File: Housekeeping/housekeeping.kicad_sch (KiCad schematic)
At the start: 4 parts, among them P7803B-1000R1 P7803B-1000, P7812B-1000R1 490-P7812B-1000

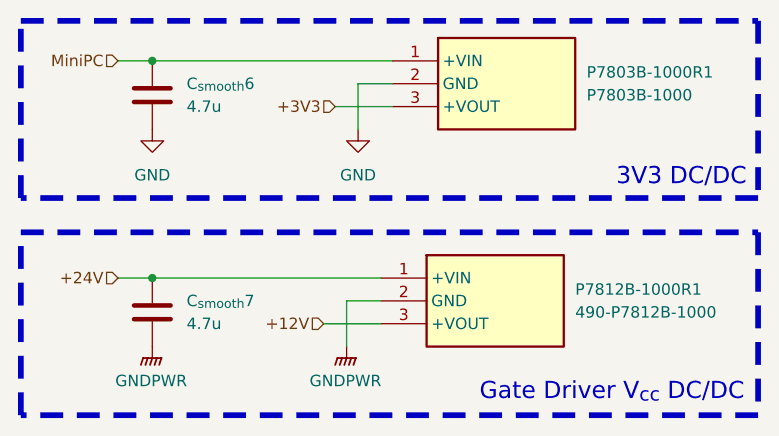
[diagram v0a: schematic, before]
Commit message: still need to finish housekeeping power supply footprints
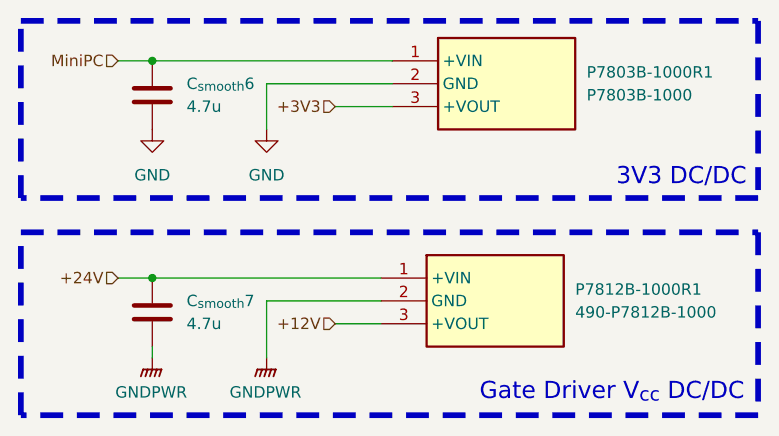
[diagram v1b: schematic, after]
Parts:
- P7803B-1000R1, P7812B-1000R1: footprint Robomaster_ICs:P7812B1000 -> Robomaster_ICs:P78B-1000R
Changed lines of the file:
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@@
 	(wire
 		(pts
-			(xy 130.81 106.68) (xy 130.81 101.6)
+			(xy 121.92 107.95) (xy 121.92 101.6)
 		)
 		(stroke
@@
 	(wire
 		(pts
-			(xy 132.08 77.47) (xy 132.08 82.55)
-		)
-		(stroke
-			(width 0)
-			(type default)
-		)
-	)
-	(wire
-		(pts
-			(xy 135.89 77.47) (xy 132.08 77.47)
-		)
-		(stroke
-			(width 0)
-			(type default)
-		)
-	)
-	(wire
-		(pts
-			(xy 128.27 104.14) (xy 134.62 104.14)
+			(xy 121.92 77.47) (xy 121.92 82.55)
+		)
+		(stroke
+			(width 0)
+			(type default)
+		)
+	)
+	(wire
+		(pts
+			(xy 135.89 77.47) (xy 121.92 77.47)
+		)
+		(stroke
+			(width 0)
+			(type default)
+		)
+	)
+	(wire
+		(pts
+			(xy 109.22 107.95) (xy 109.22 106.68)
+		)
+		(stroke
+			(width 0)
+			(type default)
+		)
+	)
+	(wire
+		(pts
+			(xy 129.54 104.14) (xy 134.62 104.14)
 		)
 		(stroke
@@
 	(wire
 		(pts
-			(xy 130.81 101.6) (xy 134.62 101.6)
+			(xy 121.92 101.6) (xy 134.62 101.6)
 		)
 		(stroke
@@
 	(hierarchical_label "+12V"
 		(shape input)
-		(at 128.27 104.14 180)
+		(at 129.54 104.14 180)
 		(effects
 			(font
@@
 	(symbol
 		(lib_id "power:GNDPWR")
-		(at 109.22 106.68 0)
+		(at 109.22 107.95 0)
 		(unit 1)
 		(exclude_from_sim no)
@@
 		(fields_autoplaced yes)
 		(property "Reference" "#PWR035"
-			(at 109.22 111.76 0)
+			(at 109.22 113.03 0)
 			(effects
 				(font
@@
 		)
 		(property "Value" "GNDPWR"
-			(at 109.093 110.49 0)
+			(at 109.093 111.76 0)
 			(effects
 				(font
@@
 		)
 		(property "Footprint" ""
+			(at 109.22 109.22 0)
+			(effects
+				(font
+					(size 1.27 1.27)
+				)
+				(hide yes)
+			)
+		)
+		(property "Datasheet" ""
+			(at 109.22 109.22 0)
+			(effects
+				(font
+					(size 1.27 1.27)
+				)
+				(hide yes)
+			)
+		)
+		(property "Description" "Power symbol creates a global label with name \"GNDPWR\" , global ground"
 			(at 109.22 107.95 0)
-			(effects
-				(font
-					(size 1.27 1.27)
-				)
-				(hide yes)
-			)
-		)
-		(property "Datasheet" ""
-			(at 109.22 107.95 0)
-			(effects
-				(font
-					(size 1.27 1.27)
-				)
-				(hide yes)
-			)
-		)
-		(property "Description" "Power symbol creates a global label with name \"GNDPWR\" , global ground"
-			(at 109.22 106.68 0)
 			(effects
 				(font
@@
 	(symbol
 		(lib_id "power:GNDPWR")
-		(at 130.81 106.68 0)
+		(at 121.92 107.95 0)
 		(unit 1)
 		(exclude_from_sim no)
@@
 		(fields_autoplaced yes)
 		(property "Reference" "#PWR021"
-			(at 130.81 111.76 0)
+			(at 121.92 113.03 0)
 			(effects
 				(font
@@
 		)
 		(property "Value" "GNDPWR"
-			(at 130.683 110.49 0)
+			(at 121.793 111.76 0)
 			(effects
 				(font
@@
 		)
 		(property "Footprint" ""
-			(at 130.81 107.95 0)
+			(at 121.92 109.22 0)
 			(effects
 				(font
@@
 		)
 		(property "Datasheet" ""
-			(at 130.81 107.95 0)
+			(at 121.92 109.22 0)
 			(effects
 				(font
@@
 		)
 		(property "Description" "Power symbol creates a global label with name \"GNDPWR\" , global ground"
-			(at 130.81 106.68 0)
+			(at 121.92 107.95 0)
 			(effects
 				(font
@@
 	(symbol
 		(lib_id "power:GND")
-		(at 132.08 82.55 0)
+		(at 121.92 82.55 0)
 		(unit 1)
 		(exclude_from_sim no)
@@
 		(fields_autoplaced yes)
 		(property "Reference" "#PWR022"
-			(at 132.08 88.9 0)
+			(at 121.92 88.9 0)
 			(effects
 				(font
@@
 		)
 		(property "Value" "GND"
-			(at 132.08 87.63 0)
+			(at 121.92 87.63 0)
 			(effects
 				(font
@@
 		)
 		(property "Footprint" ""
-			(at 132.08 82.55 0)
+			(at 121.92 82.55 0)
 			(effects
 				(font
@@
 		)
 		(property "Datasheet" ""
-			(at 132.08 82.55 0)
+			(at 121.92 82.55 0)
 			(effects
 				(font
@@
 		)
 		(property "Description" "Power symbol creates a global label with name \"GND\" , ground"
-			(at 132.08 82.55 0)
+			(at 121.92 82.55 0)
 			(effects
 				(font
@@
 			)
 		)
-		(property "Footprint" "Robomaster_ICs:P7812B1000"
+		(property "Footprint" "Robomaster_ICs:P78B-1000R"
 			(at 156.21 193.98 0)
 			(effects
@@
 			)
 		)
-		(property "Footprint" "Robomaster_ICs:P7812B1000"
+		(property "Footprint" "Robomaster_ICs:P78B-1000R"
 			(at 157.48 169.85 0)
 			(effects

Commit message: cleaned up PCB after meeting with BBJ
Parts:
- PSU_{24V}1: renamed from P7812B-1000R1; footprint Robomaster_ICs:P78B-1000R -> Robomaster_ICs:P7812B1000
- PSU_{3V3}1: renamed from P7803B-1000R1; footprint Robomaster_ICs:P78B-1000R -> Robomaster_ICs:P7812B1000
- renumbered C_{smooth}6 to C_{smooth}4, C_{smooth}7 to C_{smooth}5
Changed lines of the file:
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@@
 		(dnp no)
 		(fields_autoplaced yes)
-		(property "Reference" "C_{smooth}7"
+		(property "Reference" "C_{smooth}5"
 			(at 113.03 101.5999 0)
 			(effects
@@
 			(project "Supercap"
 				(path "/98ee8313-37ab-4329-91ab-b5710476f82f/47f13d7b-df0e-4361-81b8-c133778882c5"
-					(reference "C_{smooth}7")
+					(reference "C_{smooth}5")
 					(unit 1)
 				)
@@
 		(dnp no)
 		(fields_autoplaced yes)
-		(property "Reference" "#PWR035"
+		(property "Reference" "#PWR024"
 			(at 109.22 113.03 0)
 			(effects
@@
 			(project "Supercap"
 				(path "/98ee8313-37ab-4329-91ab-b5710476f82f/47f13d7b-df0e-4361-81b8-c133778882c5"
-					(reference "#PWR035")
+					(reference "#PWR024")
 					(unit 1)
 				)
@@
 		(dnp no)
 		(fields_autoplaced yes)
-		(property "Reference" "#PWR021"
+		(property "Reference" "#PWR026"
 			(at 121.92 113.03 0)
 			(effects
@@
 			(project "Supercap"
 				(path "/98ee8313-37ab-4329-91ab-b5710476f82f/47f13d7b-df0e-4361-81b8-c133778882c5"
-					(reference "#PWR021")
+					(reference "#PWR026")
 					(unit 1)
 				)
@@
 		(dnp no)
 		(fields_autoplaced yes)
-		(property "Reference" "#PWR022"
+		(property "Reference" "#PWR025"
 			(at 121.92 88.9 0)
 			(effects
@@
 			(project "Supercap"
 				(path "/98ee8313-37ab-4329-91ab-b5710476f82f/47f13d7b-df0e-4361-81b8-c133778882c5"
-					(reference "#PWR022")
+					(reference "#PWR025")
 					(unit 1)
 				)
@@
 		(dnp no)
 		(fields_autoplaced yes)
-		(property "Reference" "P7812B-1000R1"
+		(property "Reference" "PSU_{24V}1"
 			(at 156.21 100.3299 0)
 			(effects
@@
 			)
 		)
-		(property "Footprint" "Robomaster_ICs:P78B-1000R"
+		(property "Footprint" "Robomaster_ICs:P7812B1000"
 			(at 156.21 193.98 0)
 			(effects
@@
 			(project "Supercap"
 				(path "/98ee8313-37ab-4329-91ab-b5710476f82f/47f13d7b-df0e-4361-81b8-c133778882c5"
-					(reference "P7812B-1000R1")
+					(reference "PSU_{24V}1")
 					(unit 1)
 				)
@@
 		(dnp no)
 		(fields_autoplaced yes)
-		(property "Reference" "C_{smooth}6"
+		(property "Reference" "C_{smooth}4"
 			(at 113.03 77.4699 0)
 			(effects
@@
 			(project "Supercap"
 				(path "/98ee8313-37ab-4329-91ab-b5710476f82f/47f13d7b-df0e-4361-81b8-c133778882c5"
-					(reference "C_{smooth}6")
+					(reference "C_{smooth}4")
 					(unit 1)
 				)
@@
 		(dnp no)
 		(fields_autoplaced yes)
-		(property "Reference" "#PWR034"
+		(property "Reference" "#PWR023"
 			(at 109.22 88.9 0)
 			(effects
@@
 			(project "Supercap"
 				(path "/98ee8313-37ab-4329-91ab-b5710476f82f/47f13d7b-df0e-4361-81b8-c133778882c5"
-					(reference "#PWR034")
+					(reference "#PWR023")
 					(unit 1)
 				)
@@
 		(dnp no)
 		(fields_autoplaced yes)
-		(property "Reference" "P7803B-1000R1"
+		(property "Reference" "PSU_{3V3}1"
 			(at 157.48 76.1999 0)
 			(effects
@@
 			)
 		)
-		(property "Footprint" "Robomaster_ICs:P78B-1000R"
+		(property "Footprint" "Robomaster_ICs:P7812B1000"
 			(at 157.48 169.85 0)
 			(effects
@@
 			(project "Supercap"
 				(path "/98ee8313-37ab-4329-91ab-b5710476f82f/47f13d7b-df0e-4361-81b8-c133778882c5"
-					(reference "P7803B-1000R1")
-					(unit 1)
-				)
+					(reference "PSU_{3V3}1")
+					(unit 1)
+				)
